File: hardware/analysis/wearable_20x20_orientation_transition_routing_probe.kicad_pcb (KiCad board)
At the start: 4 copper layers, 49.3 x 49.3 mm, 400 parts

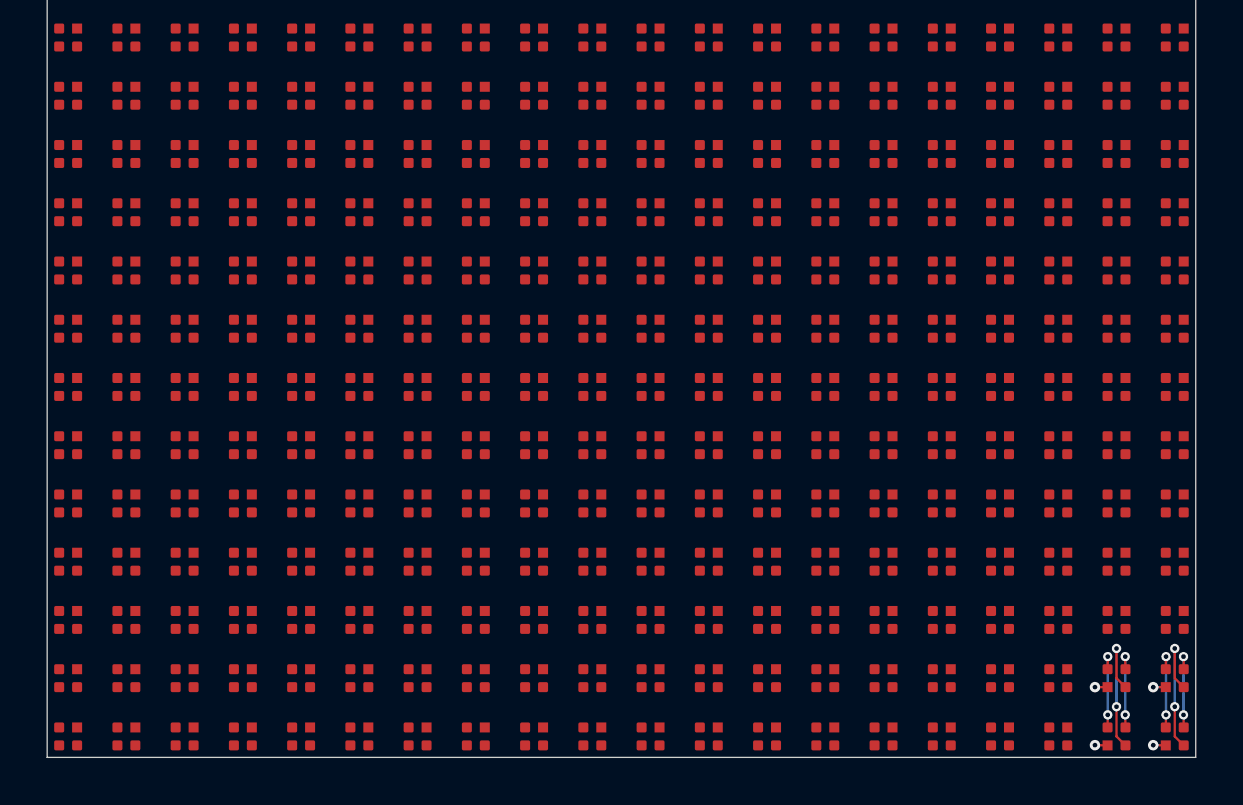
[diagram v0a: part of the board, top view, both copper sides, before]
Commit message: Validate matrix orientation transition routing
Co-authored-by: illiapliukhin <illiapliukhin@users.noreply.github.com>
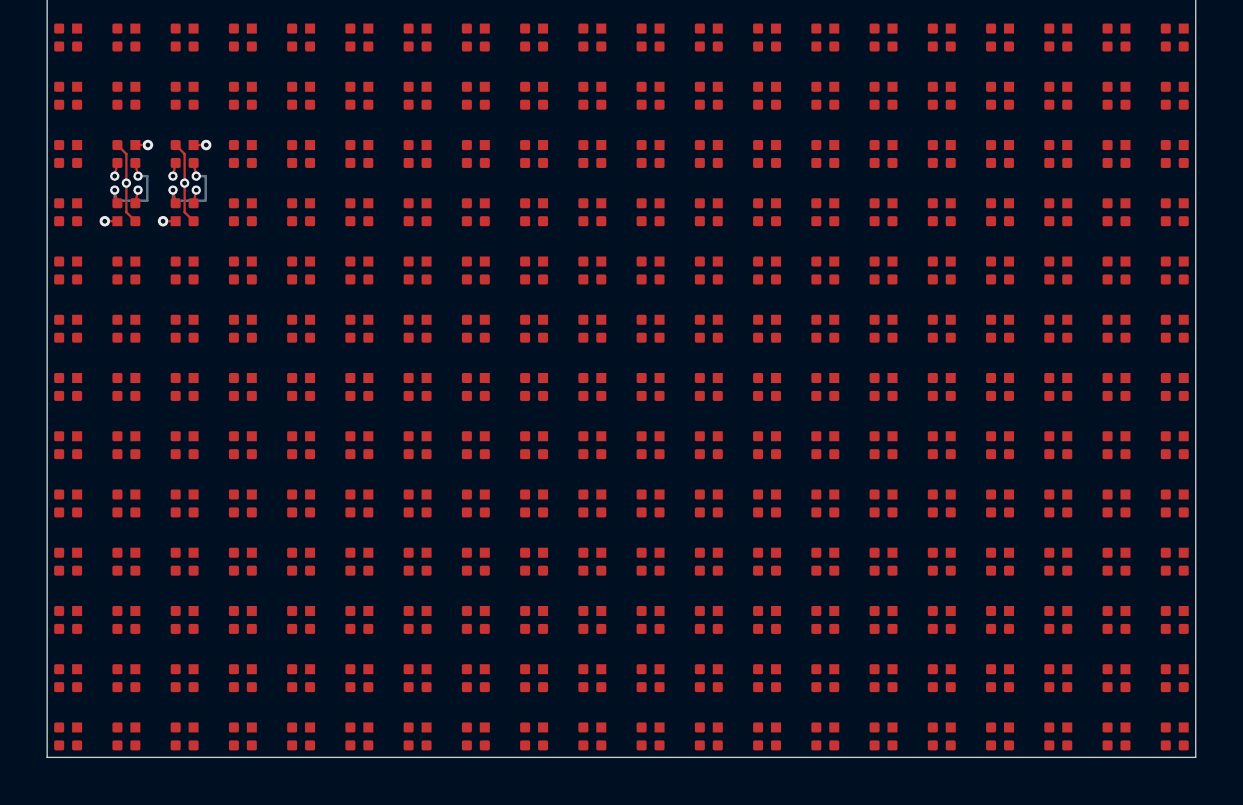
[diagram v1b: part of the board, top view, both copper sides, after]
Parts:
- turned D202 to 180 degrees
- turned D203 to 180 degrees
- turned D379 to 0 degrees
- turned D380 to 0 degrees
- turned D399 to 0 degrees
- turned D400 to 0 degrees
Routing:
- net COL_B_20: track 6.14 -> 0.00 mm, vias 2 -> 0
- net COL_B_19: track 6.14 -> 0.00 mm, vias 2 -> 0
- net COL_G_03: track 0.00 -> 4.45 mm, vias 0 -> 2
- net COL_G_02: track 0.00 -> 4.45 mm, vias 0 -> 2
- net COL_R_03: track 0.00 -> 4.45 mm, vias 0 -> 2
- net COL_R_02: track 0.00 -> 4.45 mm, vias 0 -> 2
- net ROW_11_ANODE: track 0.00 -> 4.35 mm, vias 0 -> 2
- net ROW_10_ANODE: track 0.00 -> 4.35 mm, vias 0 -> 2
- net ROW_19_ANODE: track 4.35 -> 0.00 mm, vias 2 -> 0
- net COL_B_02: track 0.00 -> 3.79 mm, vias 0 -> 1
- net COL_B_03: track 0.00 -> 3.79 mm, vias 0 -> 1
- net ROW_20_ANODE: track 3.58 -> 0.00 mm, vias 2 -> 0
- net COL_R_20: track 3.58 -> 0.00 mm, vias 2 -> 0
- net COL_R_19: track 3.58 -> 0.00 mm, vias 2 -> 0
- net COL_G_20: track 3.58 -> 0.00 mm, vias 2 -> 0
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
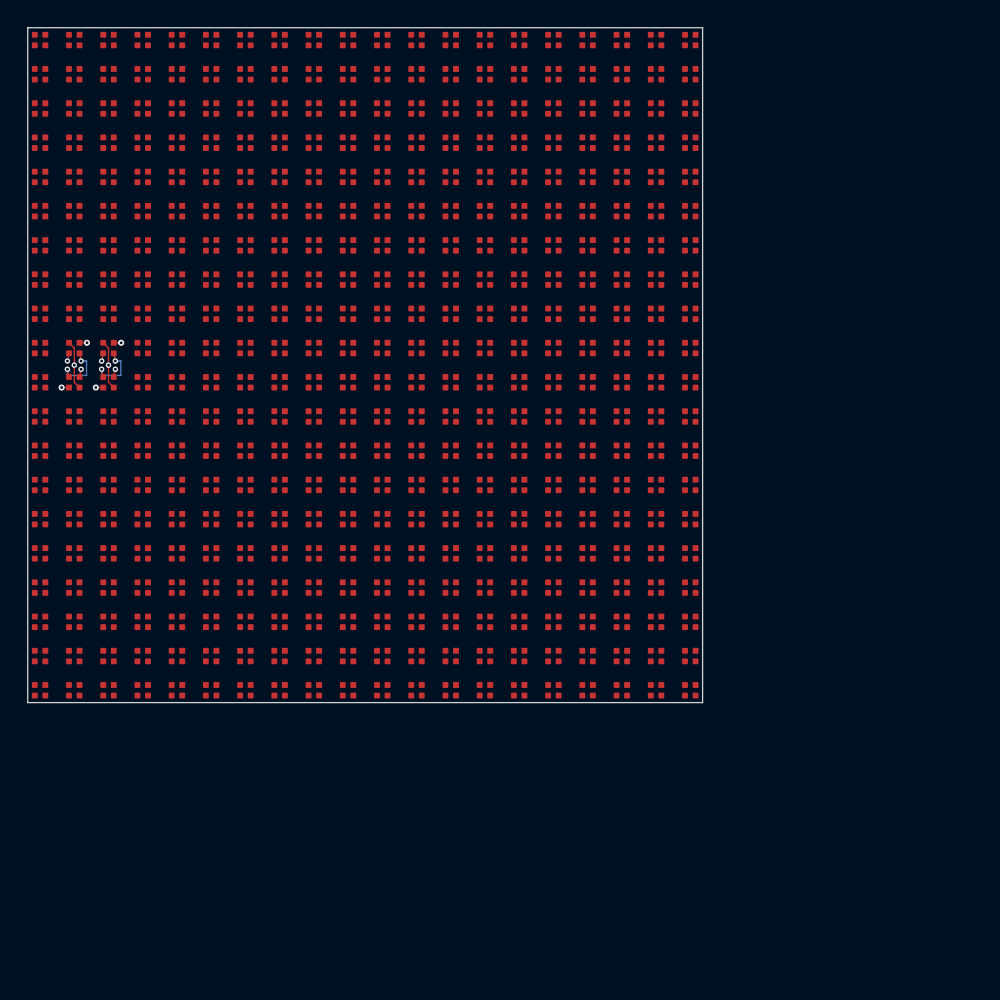
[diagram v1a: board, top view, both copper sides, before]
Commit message: Place 20x20 backside parts outside the via field
Co-authored-by: illiapliukhin <illiapliukhin@users.noreply.github.com>
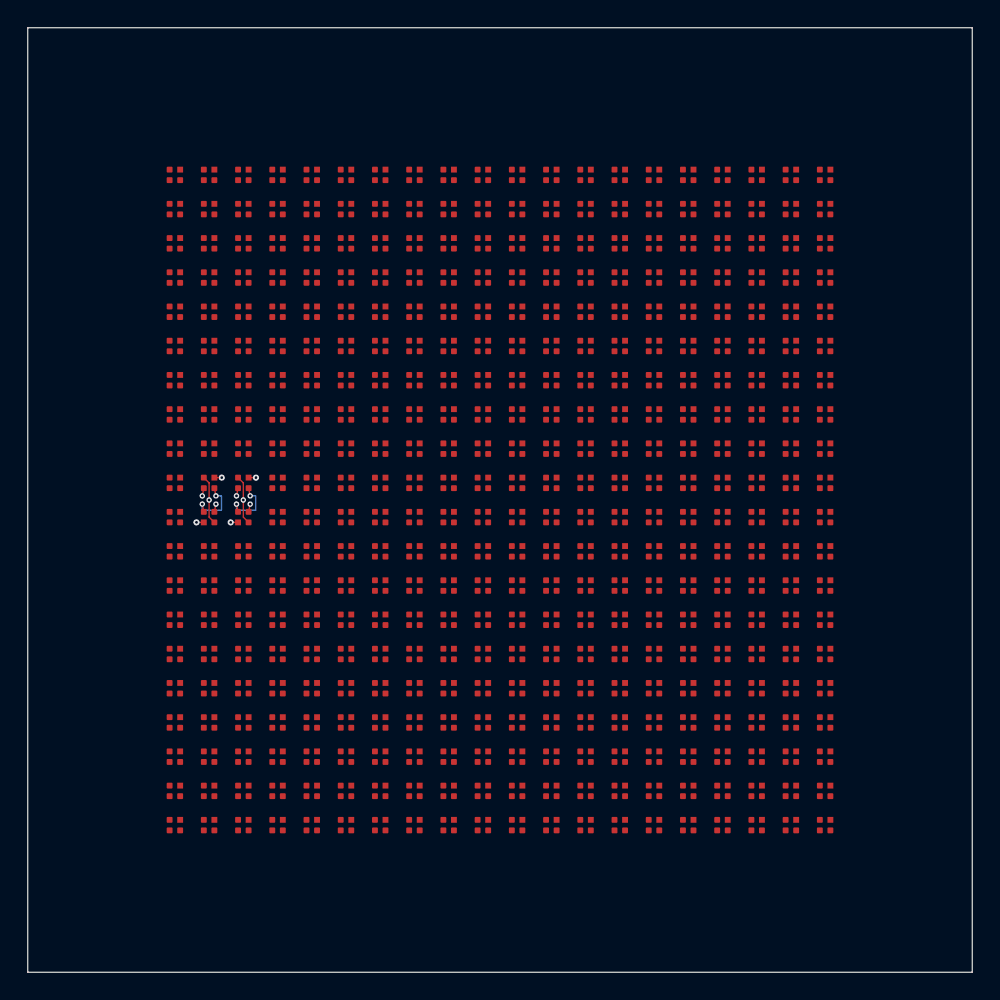
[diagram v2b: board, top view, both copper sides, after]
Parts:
- moved D1 13.9 mm to (10.8, 10.8)
- moved D101 13.9 mm to (10.8, 23.2)
- moved D104 13.9 mm to (18.2, 23.2)
- moved D105 13.9 mm to (20.8, 23.2)
- moved D106 13.9 mm to (23.2, 23.2)
- moved D107 13.9 mm to (25.8, 23.2)
- moved D121 13.9 mm to (10.8, 25.8)
- moved D124 13.9 mm to (18.2, 25.8)
- moved D125 13.9 mm to (20.8, 25.8)
- moved D126 13.9 mm to (23.2, 25.8)
- moved D127 13.9 mm to (25.8, 25.8)
- moved D4 13.9 mm to (18.2, 10.8)
- moved D5 13.9 mm to (20.8, 10.8)
- moved D6 13.9 mm to (23.2, 10.8)
- moved D61 13.9 mm to (10.8, 18.2)
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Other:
- board size 49.3 x 49.3 mm -> 69 x 69 mm
